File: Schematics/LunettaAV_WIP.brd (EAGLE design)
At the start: 129.5 x 138.4 mm, 98 parts, among them IC1 TLC339P

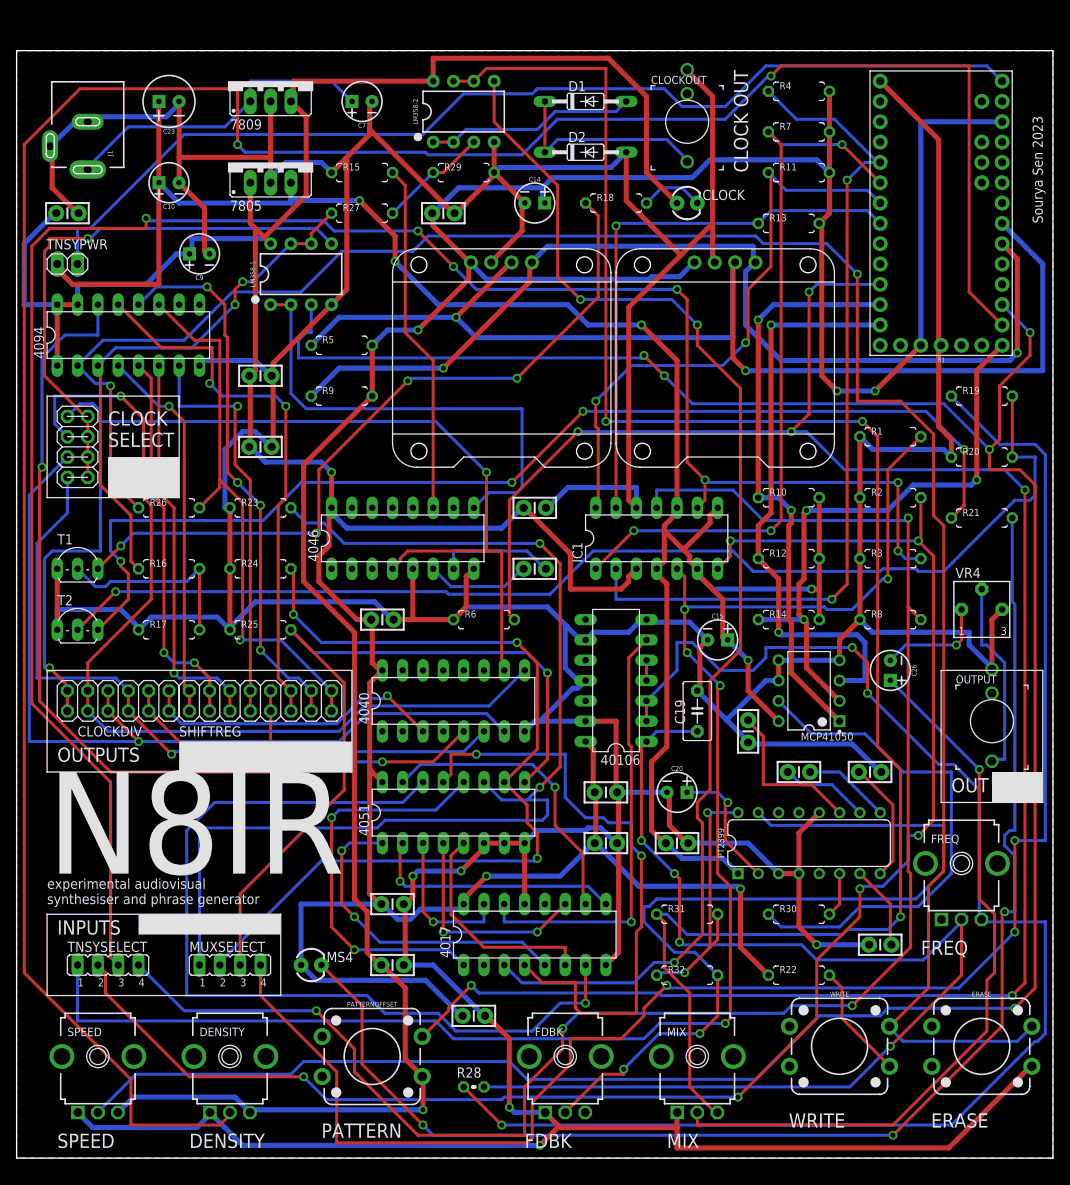
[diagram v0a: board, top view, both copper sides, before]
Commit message: redesign board for mounting holes
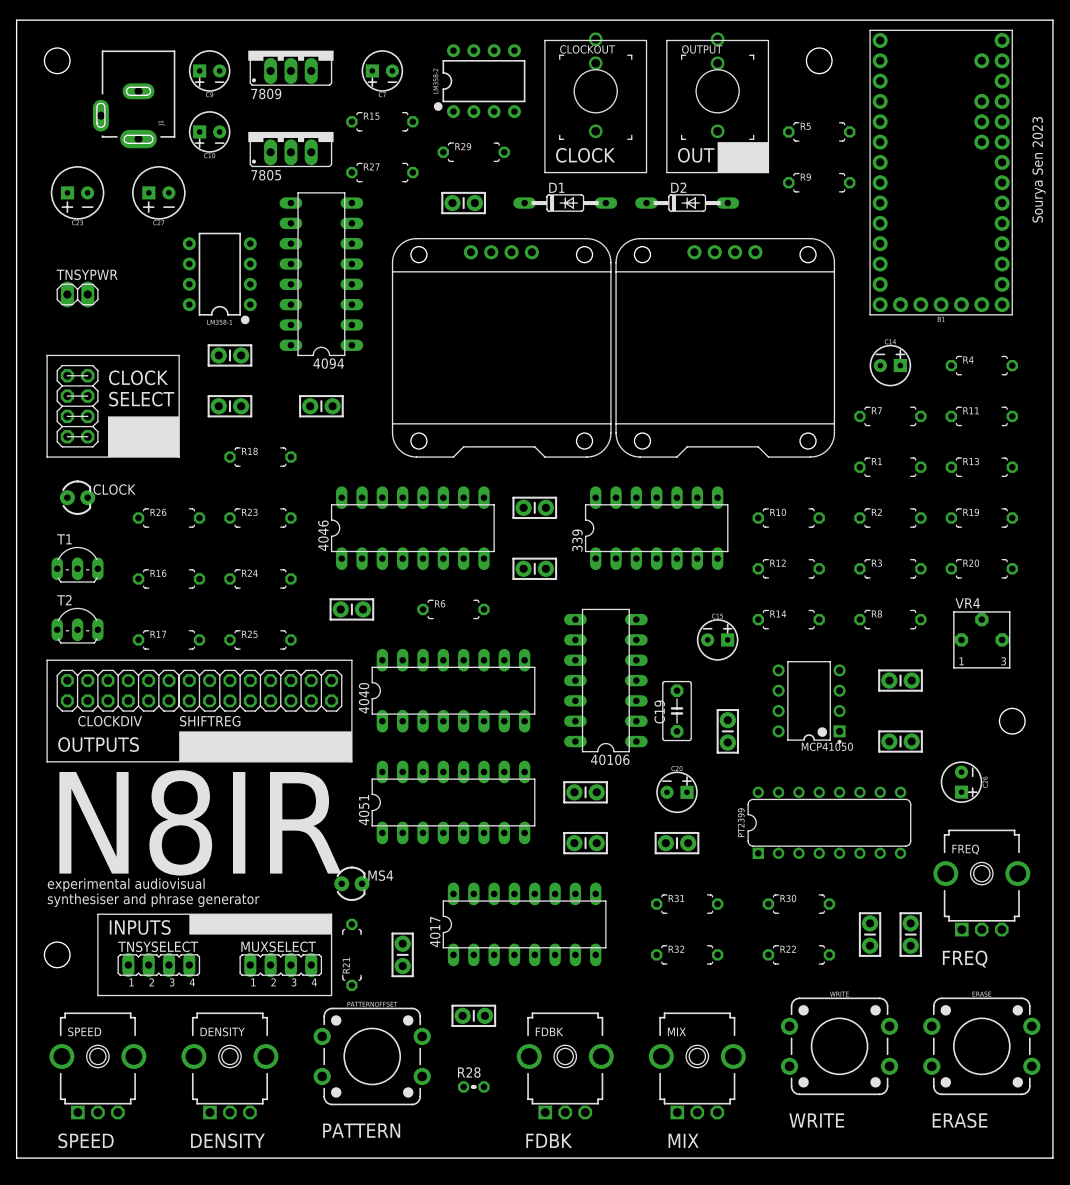
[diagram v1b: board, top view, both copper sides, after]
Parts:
- removed IC1: TLC339P, linear:DIL14
- added 339: TLC339P, linear:DIL14
- added C27: 100uF, SparkFun-Capacitors:CPOL-RADIAL-2.5MM-6.5MM
- added U$1, U$2, U$3, U$4: (no value), MusicThingModular:MOUNTING_HOLE
- moved R21 95.8 mm to (41.9, 25.4), turned to 90 degrees
- moved OUTPUT 85.9 mm to (87.6, 133.3)
- moved CLOCK 84.6 mm to (7.62, 82.5)
- moved C13 66.7 mm to (110.5, 52.1)
- moved R5 65.4 mm to (100.3, 128.3)
- moved R9 65.4 mm to (100.3, 121.9)
- moved R18 54.6 mm to (30.5, 87.6)
- moved C14 48.9 mm to (109.2, 99.1)
- moved R4 41.2 mm to (120.7, 99.1)
- moved C12 39.9 mm to (38.1, 94.0)
- moved R13 38.9 mm to (120.7, 86.4)
- moved R11 38.1 mm to (120.7, 92.7)
- moved R7 37.4 mm to (109.2, 92.7)
- moved 4094 25.3 mm to (38.1, 110.5), turned to 90 degrees
- moved C9 22.9 mm to (24.1, 135.9)
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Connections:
- net 5V: now also 339.10, 339.4, 339.6, 339.8; no longer IC1.10, IC1.4, IC1.6, IC1.8
- net 9V: now also 339.3, C27.1; no longer IC1.3
- net GND: now also 339.12, C27.2; no longer IC1.12
- net OOX: now also 339.11; no longer IC1.11
- net OXO: now also 339.9; no longer IC1.9
- net RESET: now also 339.5; no longer IC1.5
- net TNSYOOX: now also 339.13; no longer IC1.13
- net TNSYOXO: now also 339.14; no longer IC1.14
- net TNSYRES: now also 339.2; no longer IC1.2
- net TNSYXOO: now also 339.1; no longer IC1.1
- net XOO: now also 339.7; no longer IC1.7
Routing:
- net GND: track 946.0 -> 0.00 mm, vias 5 -> 0
- net 9V: track 422.8 -> 0.00 mm, vias 3 -> 0
- net 3V3: track 346.5 -> 0.00 mm, vias 4 -> 0
- net SPEEDPIN: track 318.1 -> 0.00 mm, vias 5 -> 0
- net DENSITYPIN: track 308.5 -> 0.00 mm, vias 2 -> 0
- net 5V: track 258.7 -> 0.00 mm, vias 5 -> 0
- net BOUNCEPIN: track 254.8 -> 0.00 mm, vias 6 -> 0
- net N$28: track 251.9 -> 0.00 mm, vias 2 -> 0
- net OXO: track 246.1 -> 0.00 mm, vias 7 -> 0
- net BUFFMEL: track 220.3 -> 0.00 mm, vias 3 -> 0
- net OOX: track 213.2 -> 0.00 mm, vias 4 -> 0
- net LDRIVER: track 205.4 -> 0.00 mm, vias 3 -> 0
- net XOO: track 204.5 -> 0.00 mm, vias 6 -> 0
- net RESET: track 196.5 -> 0.00 mm, vias 5 -> 0
- net N$9: track 180.3 -> 0.00 mm, vias 3 -> 0
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- removed copper zone on layer 1, net GND
- removed copper zone on layer 16, net GND
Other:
- board size 129.5 x 138.4 mm -> 129.5 x 142.2 mm
- board text added: "CLOCK"
- board text removed: "CLOCK OUT"

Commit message: more changes and gerber for ordering
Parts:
- C7: value 10uF -> 100uF; device SparkFun-Capacitors:CPOL-RADIAL-2.5MM-5MM -> SparkFun-Capacitors:CPOL-RADIAL-2.5MM-6.5MM
- moved C7 44.9 mm to (6.35, 114.3)
- moved CLOCK 24.1 mm to (15.2, 105.4)
- moved TNSYPWR 22.6 mm to (21.6, 125.7)
- moved C27 19.1 mm to (6.35, 105.4)
- moved C10 11.7 mm to (15.2, 135.9)
- moved C23 9.92 mm to (15.2, 114.3)
- moved J1 9.92 mm to (8.89, 125.7), turned to 180 degrees
- moved T1 6.35 mm to (7.62, 81.3)
- moved R15 5.08 mm to (45.7, 134.6)
- moved C15 2.84 mm to (86.4, 67.3)
- moved C19 2.84 mm to (85.1, 57.1)
- moved C24 2.84 mm to (90.2, 50.8)
- moved LM358-1 2.54 mm to (25.4, 113.0)
- moved R27 2.54 mm to (45.7, 125.7)
- moved T2 2.54 mm to (7.62, 69.8)
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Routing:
- net GND: track 0.00 -> 1029.4 mm, vias 0 -> 1
- net 9V: track 0.00 -> 442.2 mm, vias 0 -> 1
- net 3V3: track 0.00 -> 425.9 mm, vias 0 -> 2
- net 5V: track 0.00 -> 272.6 mm, vias 0 -> 2
- net OXO: track 0.00 -> 250.4 mm, vias 0 -> 1
- net SPEEDPIN: track 0.00 -> 250.1 mm, vias 0 -> 2
- net N$28: track 0.00 -> 230.3 mm, vias 0 -> 1
- net DENSITYPIN: track 0.00 -> 208.7 mm, vias 0 -> 1
- net OOX: track 0.00 -> 205.7 mm, vias 0 -> 2
- net XOO: track 0.00 -> 191.2 mm, vias 0 -> 1
- net RESET: track 0.00 -> 172.8 mm, vias 0 -> 3
- net N$9: track 0.00 -> 168.3 mm, vias 0 -> 2
- net BOUNCEPIN: track 0.00 -> 167.2 mm, vias 0 -> 2
- net BUFFMEL: track 0.00 -> 162.8 mm, vias 0 -> 1
- net SCL: track 0.00 -> 160.7 mm
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- added copper zone on layer 1, net GND
- added copper zone on layer 16, net GND
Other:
- board text added: "this project would not be possible without the knowledge shared on the electro-music forums and previous work by andy murkin"
- board text removed: "this project wouldn't be possible without the knowledge shared on electro-music forums and previous work by andy murkin"

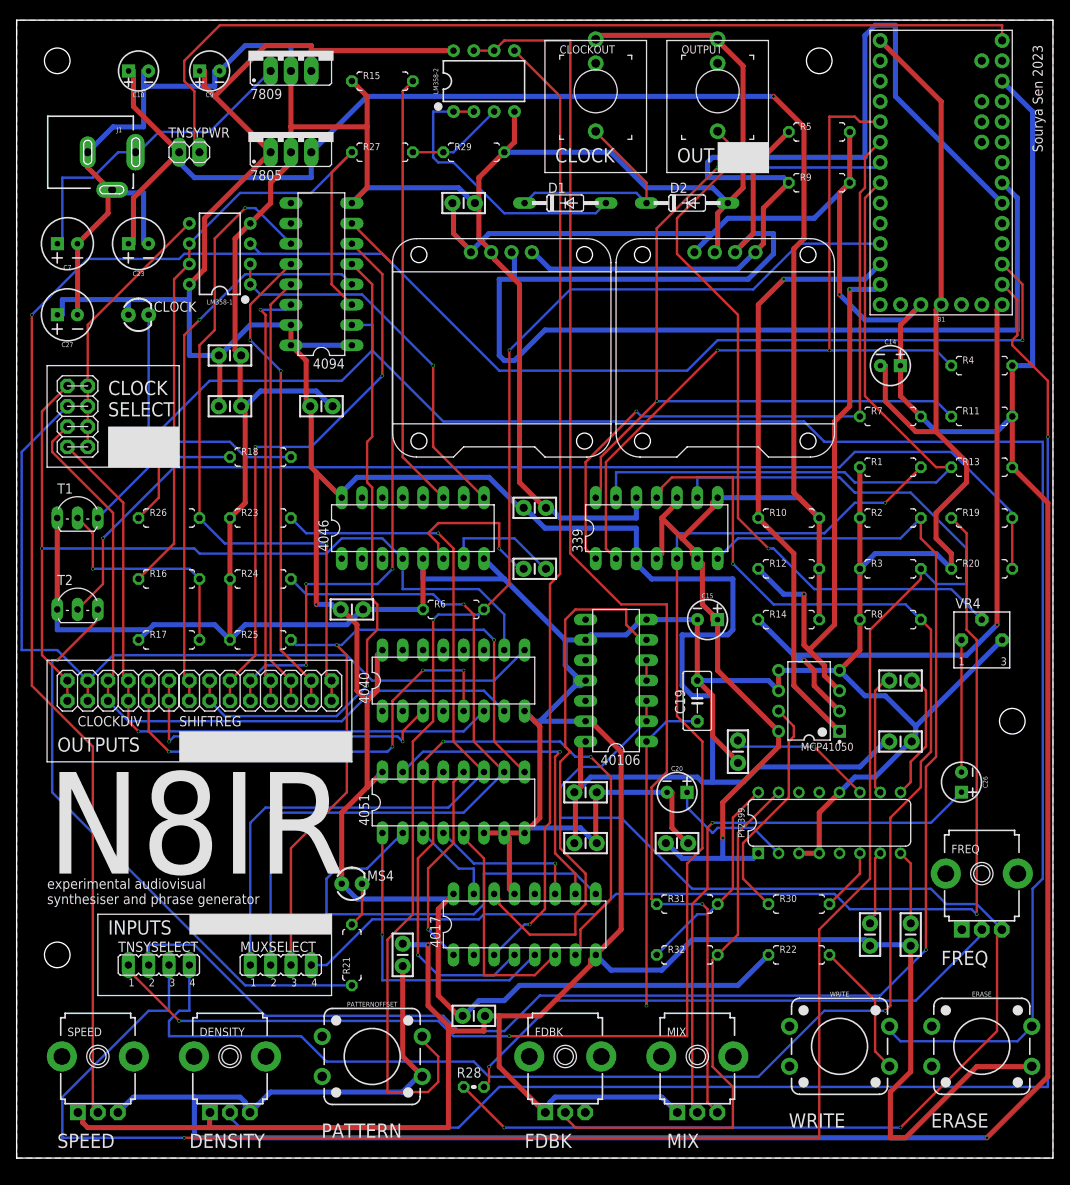
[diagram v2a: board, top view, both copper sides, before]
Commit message: fixes modifications and beautification for rev 2
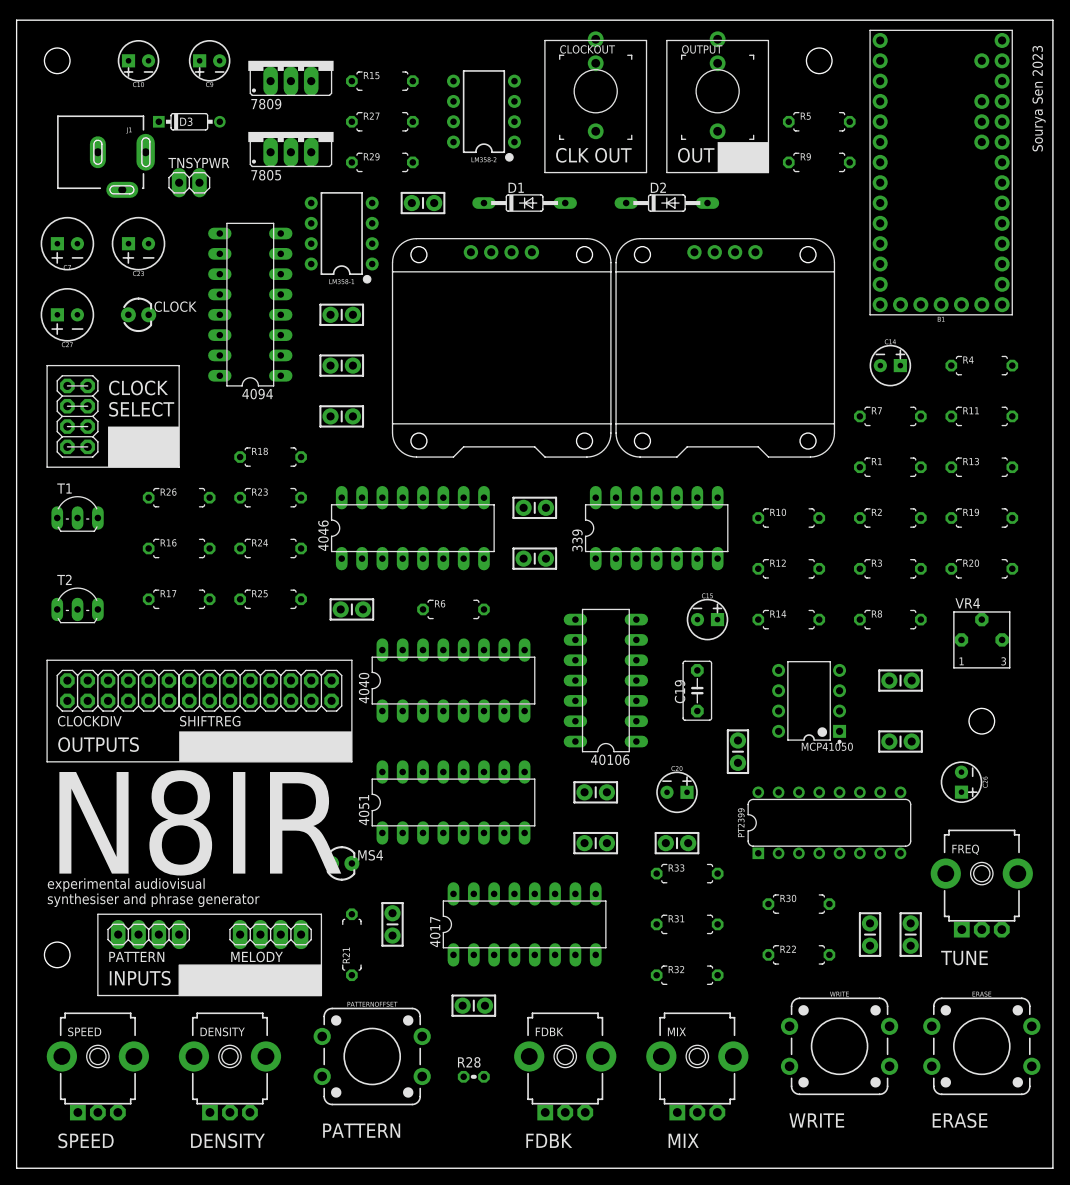
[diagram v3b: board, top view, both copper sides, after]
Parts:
- removed MUXSELECT, TNSYSELECT: (no value), jumper:JP4
- added D3: 1N4148, MusicThingModular:DO35-7
- added MELODY, PATTERN: (no value), pinhead:1X04
- added R33: 100k, MusicThingModular:7MM_RESISTOR
- C19: value 1uF -> .1uF
- moved LM358-1 15.5 mm to (40.6, 115.6)
- moved C1 14.9 mm to (40.6, 105.4)
- moved C5 14.0 mm to (40.6, 92.7)
- moved R29 11.5 mm to (45.7, 124.5)
- moved 4094 9.67 mm to (29.2, 106.7)
- moved C12 5.68 mm to (40.6, 99.1)
- moved R17 5.24 mm to (20.3, 69.8)
- moved R25 5.24 mm to (31.8, 69.8)
- moved C2 5.08 mm to (50.8, 119.4)
- moved D1 5.08 mm to (63.5, 119.4)
- moved R16 4.02 mm to (20.3, 76.2)
- moved R24 4.02 mm to (31.8, 76.2)
- moved C3 4.02 mm to (47.0, 29.2)
- moved LM358-2 3.81 mm to (58.4, 130.8), turned to 90 degrees
- moved TNSYPWR 3.81 mm to (21.6, 121.9)
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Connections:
- new net N$3: C24.1, FDBK.1, MIX.1, PT2399.12
- new net N$4: MIX.3, R33.2
- new net N$42: D3.A, J1.PWR
- net BUFFMEL: now also R33.1; no longer MIX.3
- net DCIN: now also D3.C; no longer J1.PWR
- net GND: no longer C24.1, FDBK.1, MIX.1, PT2399.12
- net LDRIVER: now also MELODY.4; no longer MUXSELECT.4
- net MOOX: now also MELODY.3; no longer MUXSELECT.3
- net MOXO: now also MELODY.2; no longer MUXSELECT.2
- net MXOO: now also MELODY.1; no longer MUXSELECT.1
- net OOX: now also PATTERN.3; no longer TNSYSELECT.4
- net OXO: now also PATTERN.2; no longer TNSYSELECT.3
- net RESET: now also PATTERN.4; no longer TNSYSELECT.1
- net XOO: now also PATTERN.1; no longer TNSYSELECT.2
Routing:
- net GND: track 1029.4 -> 0.00 mm, vias 1 -> 0
- net 9V: track 442.2 -> 0.00 mm, vias 1 -> 0
- net 3V3: track 425.9 -> 0.00 mm, vias 2 -> 0
- net 5V: track 272.6 -> 0.00 mm, vias 2 -> 0
- net OXO: track 250.4 -> 0.00 mm, vias 1 -> 0
- net SPEEDPIN: track 250.1 -> 0.00 mm, vias 2 -> 0
- net N$28: track 230.3 -> 0.00 mm, vias 1 -> 0
- net DENSITYPIN: track 208.7 -> 0.00 mm, vias 1 -> 0
- net OOX: track 205.7 -> 0.00 mm, vias 2 -> 0
- net XOO: track 191.2 -> 0.00 mm, vias 1 -> 0
- net RESET: track 172.8 -> 0.00 mm, vias 3 -> 0
- net N$9: track 168.3 -> 0.00 mm, vias 2 -> 0
- net BOUNCEPIN: track 167.2 -> 0.00 mm, vias 2 -> 0
- net BUFFMEL: track 162.8 -> 0.00 mm, vias 1 -> 0
- net SCL: track 160.7 -> 0.00 mm
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- removed copper zone on layer 1, net GND
- removed copper zone on layer 16, net GND
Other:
- board size 129.5 x 142.2 mm -> 129.5 x 143.5 mm
- board text added: "CLK OUT"
- board text added: "TUNE"
- board text removed: "CLOCK"
- board text removed: "FREQ"

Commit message: rev 2 routing
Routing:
- net GND: track 0.00 -> 900.1 mm
- net 9V: track 0.00 -> 411.8 mm, vias 0 -> 2
- net 3V3: track 0.00 -> 390.5 mm
- net SPEEDPIN: track 0.00 -> 302.0 mm
- net 5V: track 0.00 -> 252.9 mm, vias 0 -> 4
- net N$28: track 0.00 -> 218.4 mm, vias 0 -> 1
- net OOX: track 0.00 -> 215.7 mm, vias 0 -> 1
- net DENSITYPIN: track 0.00 -> 211.2 mm, vias 0 -> 1
- net OXO: track 0.00 -> 189.0 mm, vias 0 -> 2
- net BOUNCEPIN: track 0.00 -> 185.5 mm, vias 0 -> 2
- net RESET: track 0.00 -> 155.3 mm, vias 0 -> 3
- net LDRIVER: track 0.00 -> 153.9 mm
- net XOO: track 0.00 -> 147.5 mm, vias 0 -> 2
- net N$9: track 0.00 -> 147.5 mm
- net N$37: track 0.00 -> 142.4 mm, vias 0 -> 2
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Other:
- board text added: "N8IR experimental audiovisual synthesiser and phrase generator designed by sourya sen board version 1.0, revision 2"
- board text removed: "N8IR experimental audiovisual synthesiser and phrase generator designed by sourya sen board version 1.0"
